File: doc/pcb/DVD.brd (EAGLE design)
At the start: 100 x 80 mm, 26 parts, among them IC1 7805, IC2 74HC14N

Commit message: PCB Board update
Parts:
- removed R10, R8, R9: (no value), resistor:0204/7
- added BNO055_1, SD_CARD: (no value), adafruit:1X06
- added BNO055_2: (no value), pinhead:1X04
- added NRF24L01: (no value), adafruit:2X04
- added POLULU_TB6612FNG: (no value), ic-package:DIL16
- JP10: value (none) -> STBY
- JP8: value (none) -> ENGINE2
- JP9: value (none) -> ENGINE1
- moved IC1 108.9 mm to (21.9, 81.3)
- moved JP7 91.4 mm to (30.0, 78.2)
- moved R3 91.1 mm to (30.1, 65.5), turned to 90 degrees
- moved JP5 82.3 mm to (26.3, 78.2)
- moved R7 82.2 mm to (33.9, 74.6), turned to 270 degrees
- moved JP9 79.6 mm to (43.7, 44.9)
- moved C1 79.4 mm to (15.4, 77.5)
- moved JP8 76.7 mm to (43.6, 41.9)
- moved JP3 73.5 mm to (1.60, 78.8)
- moved U$1 73.2 mm to (20.1, 56.8)
- moved R6 72.6 mm to (34.1, 65.6), turned to 90 degrees
- moved JP10 71.3 mm to (43.5, 47.5)
- moved IC2 68.7 mm to (40.3, 70.2), turned to 90 degrees
- moved JP6 66.3 mm to (28.4, 78.2)
- moved VS1838 63.4 mm to (43.8, 53.5), turned to 90 degrees
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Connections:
- removed net N$12: U$1.18/A4
- removed net N$13: U$1.19/A5
- removed net N$14: U$1.21/A7
- removed net N$15: U$1.22/A8
- removed net N$16: U$1.23/A9
- removed net N$23: U$1.14/A0
- removed net N$5: U$1.9
- removed net N$6: U$1.10
- removed net N$7: U$1.11
- removed net N$8: U$1.12
- new net CE: NRF24L01.3, U$1.8
- new net CSN_RADIO: NRF24L01.4, U$1.10
- new net CSN_SD: SD_CARD.1, U$1.9
- new net ENGINE1: JP9.1, POLULU_TB6612FNG.4, POLULU_TB6612FNG.5
- new net IN1: POLULU_TB6612FNG.12, POLULU_TB6612FNG.14, U$1.23/A9
- new net IN2: POLULU_TB6612FNG.11, POLULU_TB6612FNG.15, U$1.22/A8
- new net JP8: JP8.1, POLULU_TB6612FNG.3, POLULU_TB6612FNG.6
- new net MISO: NRF24L01.7, SD_CARD.4, U$1.12
- new net MOSI: NRF24L01.6, SD_CARD.3, U$1.11
- new net PWM: POLULU_TB6612FNG.10, POLULU_TB6612FNG.16, U$1.21/A7
- new net SCK: NRF24L01.5, SD_CARD.2, U$1.14/A0
- new net SCL: BNO055_1.5, U$1.19/A5
- new net SDA: BNO055_1.4, U$1.18/A4
- net +3V3: now also BNO055_1.1, NRF24L01.2, POLULU_TB6612FNG.2
- net +5V: now also SD_CARD.5
- net GND: now also BNO055_1.3, NRF24L01.1, POLULU_TB6612FNG.1, POLULU_TB6612FNG.8, POLULU_TB6612FNG.9, SD_CARD.6
- net N$4: now also JP10.1, POLULU_TB6612FNG.13; no longer U$1.8
- net V+: now also POLULU_TB6612FNG.7
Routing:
- net N$5: track 0.00 -> 170.0 mm

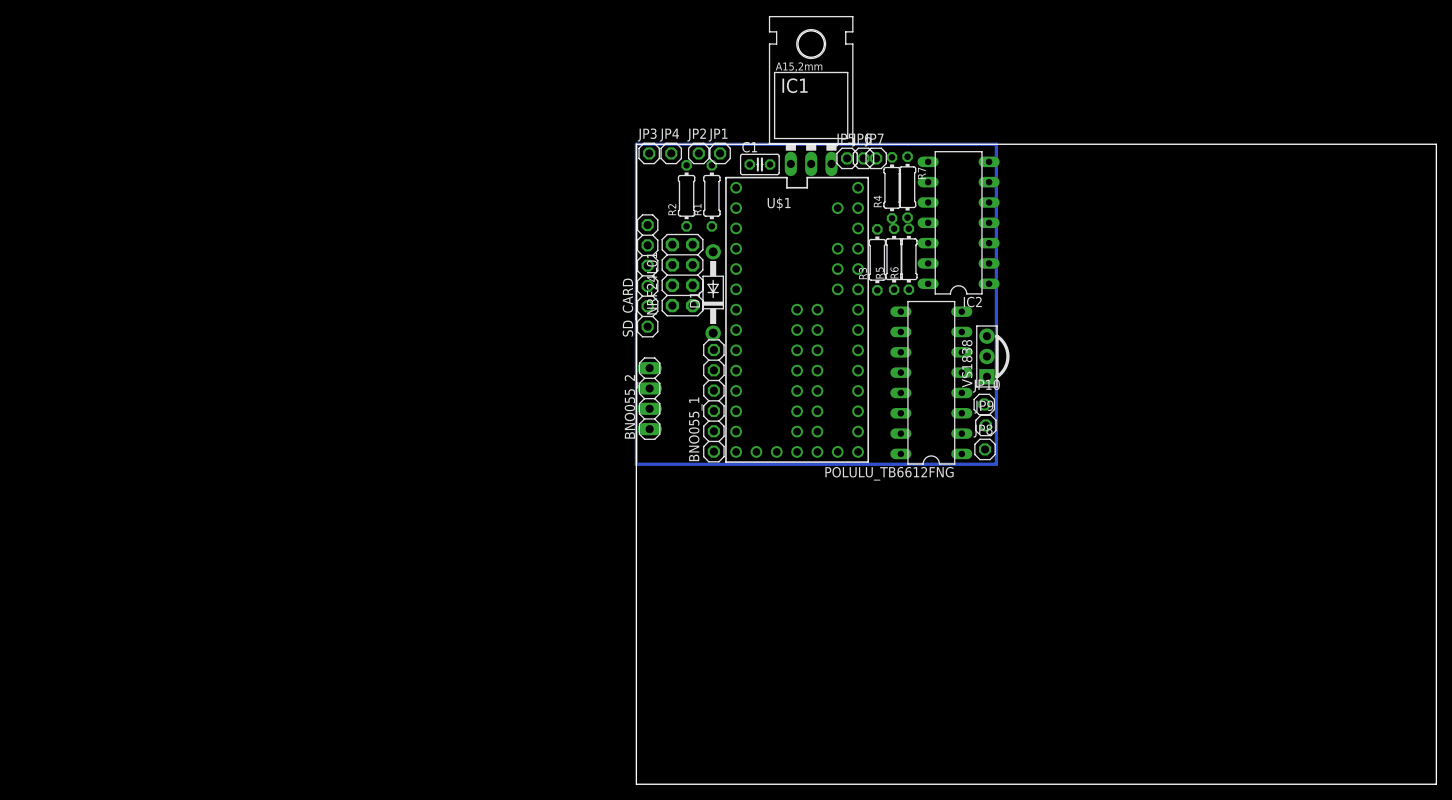
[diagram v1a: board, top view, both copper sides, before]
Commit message: Fixed Pololu/BNO055/Teensy footprint
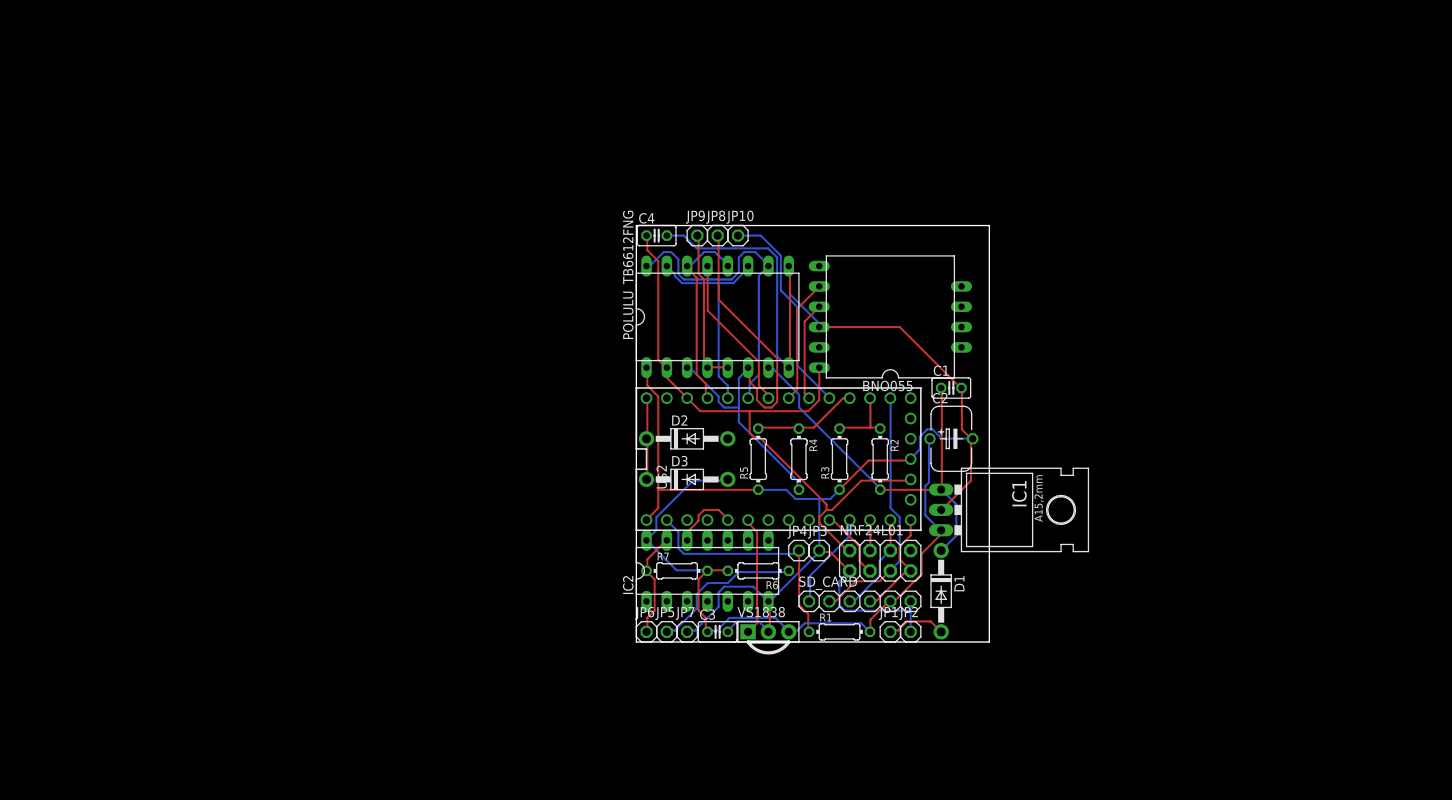
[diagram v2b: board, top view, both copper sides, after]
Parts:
- removed BNO055_1: (no value), adafruit:1X06
- removed BNO055_2: (no value), pinhead:1X04
- removed U$1: TEENSY_3.1_ALL_PINS_AND_PADS, Teensy_3_Series_Board_v1.0:TEENSY_3.1_ALLPINS
- added BNO055: (no value), ic-package_mod:DIL10-6-4
- added C2: 1000 uF, resistor:P128-50
- added C3: 100 nF, resistor:C025-025X050
- added C4: 100nF, resistor:C025-025X050
- added D2, D3: 1N4004, adafruit:DO41-10
- added U$2: TEENSY_3.1_BASIC, Teensy_3_Series_Board_v1.0:TEENSY_3.1_BASIC
- JP10: value STBY -> TEMP
- POLULU_TB6612FNG: value (none) -> DIL16W; device ic-package:DIL16 -> ic-package_mod:DIL16WIDE
- R2, R4: value 3K -> 3.3K
- moved JP2 65.4 mm to (34.3, 19.1)
- moved JP6 65.1 mm to (1.27, 19.1)
- moved JP7 63.7 mm to (6.35, 19.1)
- moved JP1 63.5 mm to (31.8, 19.1)
- moved JP5 63.3 mm to (3.81, 19.1)
- moved R1 56.8 mm to (25.4, 19.1), turned to 0 degrees
- moved R7 56.0 mm to (5.08, 26.7), turned to 0 degrees
- moved JP3 54.0 mm to (22.9, 29.2)
- moved IC2 53.7 mm to (8.89, 26.7), turned to 0 degrees
- moved JP4 52.1 mm to (20.3, 29.2)
- moved IC1 51.2 mm to (41.9, 34.3), turned to 270 degrees
- moved SD_CARD 48.6 mm to (27.9, 22.9), turned to 0 degrees
- moved D1 47.0 mm to (38.1, 24.1), turned to 270 degrees
- moved VS1838 43.9 mm to (16.5, 19.1), turned to 0 degrees
- moved NRF24L01 43.4 mm to (30.5, 27.9), turned to 0 degrees
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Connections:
- removed net AREF: U$1.AREF
- removed net N$24: U$1.17/A3
- removed net N$25: U$1.20/A6
- removed net N$29: R4.2
- removed net VCC: IC2.14
- removed net VUSB: U$1.VUSB
- new net JP0: JP10.1, U$2.17/A3
- new net N$5: D1.A, JP1.1
- new net STBY: POLULU_TB6612FNG.13, U$2.20/A6
- net +3V3: now also BNO055.1, C4.1, U$2.3.3V, U$2.3.3V1; no longer BNO055_1.1, U$1.3.3V, U$1.3.3V1, U$1.3.3V2
- net +5V: now also C2.+, C3.1, D3.A, IC2.14; no longer U$1.VIN
- net AGND: now also U$2.AGND; no longer U$1.AGND
- net CE: now also U$2.8; no longer U$1.8
- net CSN_RADIO: now also U$2.10; no longer U$1.10
- net CSN_SD: now also U$2.9; no longer U$1.9
- net D4_IR: now also U$2.4; no longer U$1.4
- net GND: now also BNO055.3, C2.-, C3.2, C4.2, U$2.GND, U$2.GND1; no longer BNO055_1.3, U$1.GND, U$1.GND1, U$1.GND2
- net IN1: now also U$2.23/A9; no longer U$1.23/A9
- net IN2: now also U$2.22/A8; no longer U$1.22/A8
- net JP8: now also R4.2
- net MISO: now also U$2.12; no longer U$1.12
- net MOSI: now also U$2.11; no longer U$1.11
- net N$1: now also D2.C, D3.C, U$2.VIN; no longer C1.1, D1.C, IC1.IN
- net N$10: now also U$2.15/A1; no longer U$1.15/A1
- net N$11: now also U$2.16/A2; no longer U$1.16/A2
- net N$18: now also U$2.0; no longer U$1.0
- net N$19: now also U$2.1; no longer U$1.1
- net N$20: now also U$2.2; no longer U$1.2
- net N$21: now also U$2.6; no longer U$1.6
- net N$22: now also U$2.7; no longer U$1.7
- net N$3: now also U$2.5; no longer U$1.5
- net N$4: now also D2.A; no longer JP10.1, POLULU_TB6612FNG.13
- net N$9: now also U$2.13; no longer U$1.13
- net PWM: now also U$2.21/A7; no longer U$1.21/A7
- net SCK: now also U$2.14/A0; no longer U$1.14/A0
- net SCL: now also BNO055.5, U$2.19/A5; no longer BNO055_1.5, U$1.19/A5
- net SDA: now also BNO055.4, U$2.18/A4; no longer BNO055_1.4, U$1.18/A4
- net SPEED_SENSOR: now also U$2.3; no longer U$1.3
- net V+: now also C1.1, D1.C, IC1.IN; no longer D1.A, JP1.1
- net VBAT: now also U$2.VBAT; no longer U$1.VBAT
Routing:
- net GND: track 0.00 -> 218.1 mm
- net N$5: track 170.0 -> 7.49 mm
- net +5V: track 0.00 -> 86.8 mm
- net +3V3: track 0.00 -> 80.6 mm
- net JP8: track 0.00 -> 59.5 mm
- net V+: track 0.00 -> 50.9 mm
- net PWM: track 0.00 -> 39.3 mm
- net SCK: track 0.00 -> 31.7 mm
- net N$18: track 0.00 -> 30.3 mm
- net IN2: track 0.00 -> 27.3 mm
- net JP0: track 0.00 -> 26.7 mm
- net IN1: track 0.00 -> 24.4 mm
- net ENGINE1: track 0.00 -> 19.8 mm
- net STBY: track 0.00 -> 19.8 mm
- net N$2: track 0.00 -> 19.5 mm
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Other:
- board size 100 x 80 mm -> 44.1 x 52.1 mm

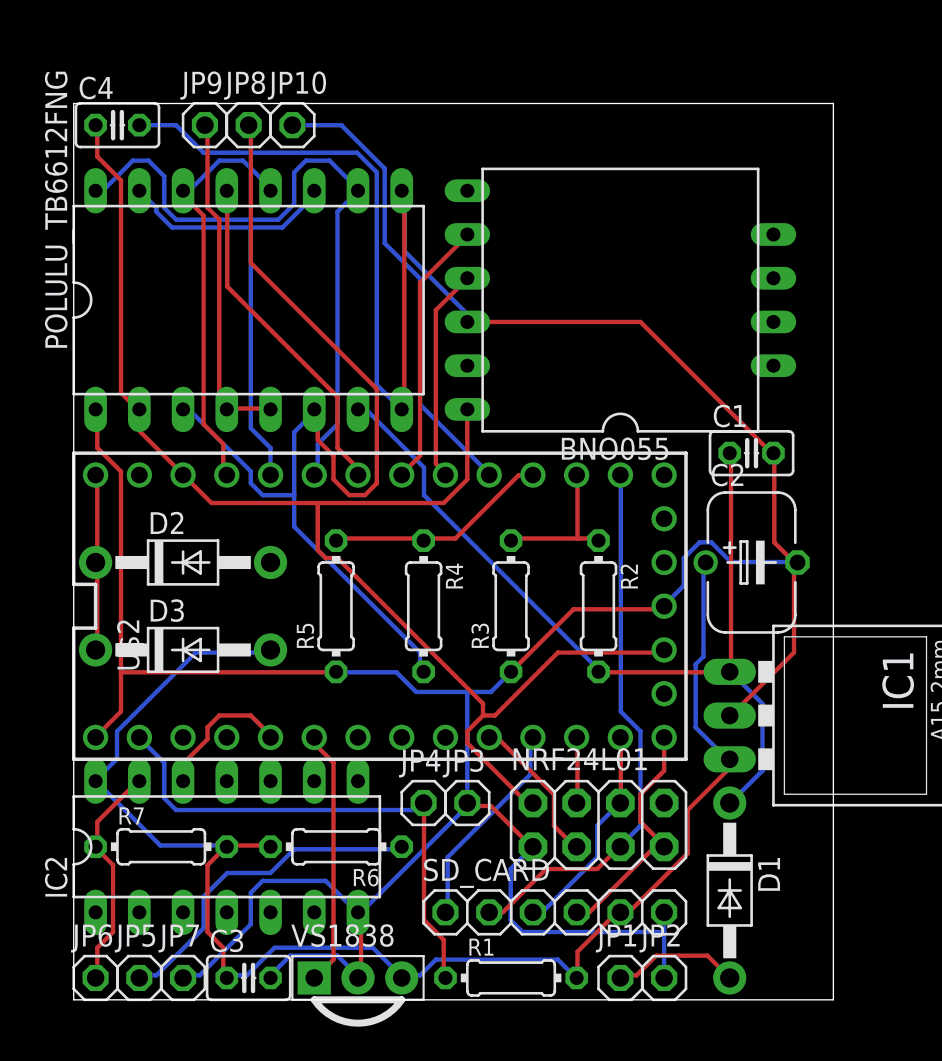
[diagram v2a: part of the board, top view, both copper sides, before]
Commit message: Fixed DR violations & added Copper Pour GND
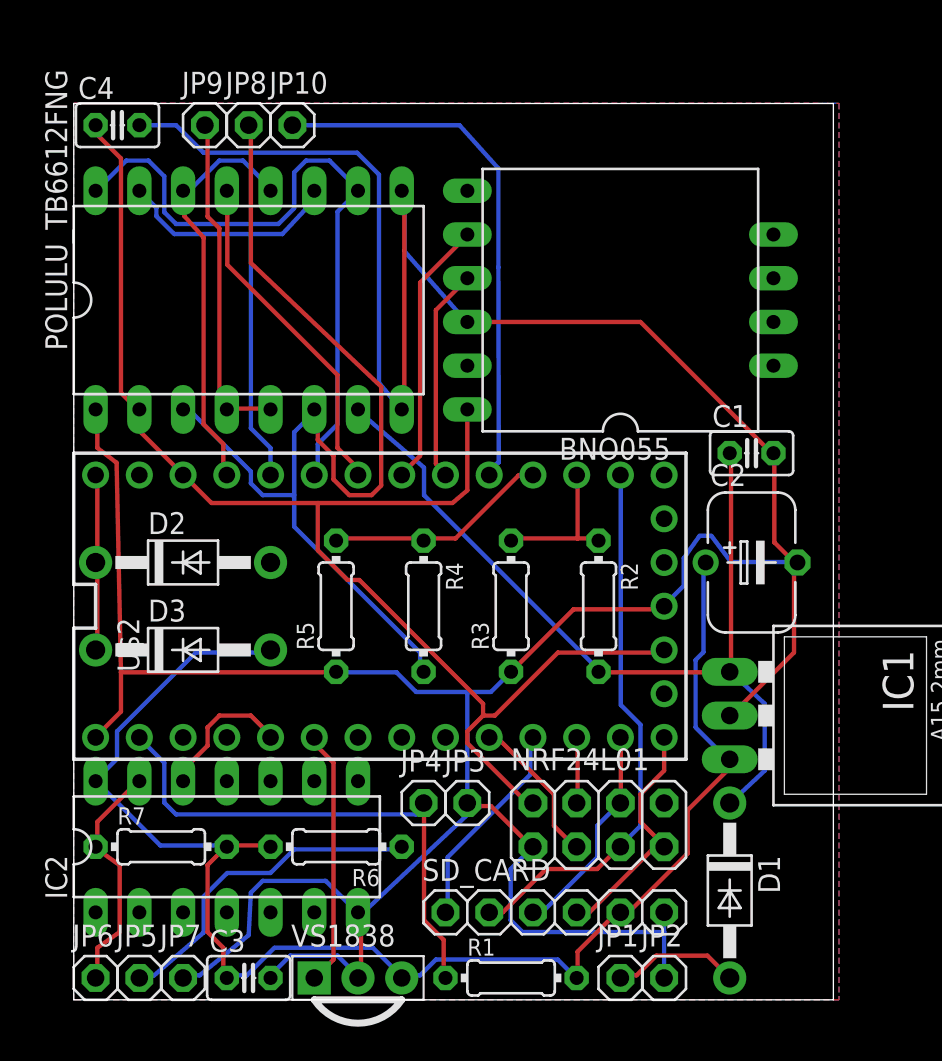
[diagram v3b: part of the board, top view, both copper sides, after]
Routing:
- net JP0: track 26.7 -> 31.3 mm
- net GND: track 218.1 -> 219.0 mm
- net N$26: track 13.3 -> 13.9 mm
- net JP8: track 59.5 -> 60.0 mm
- net PWM: track 39.3 -> 39.8 mm
- added copper zone on layer 1, net GND
- added copper zone on layer 16, net GND

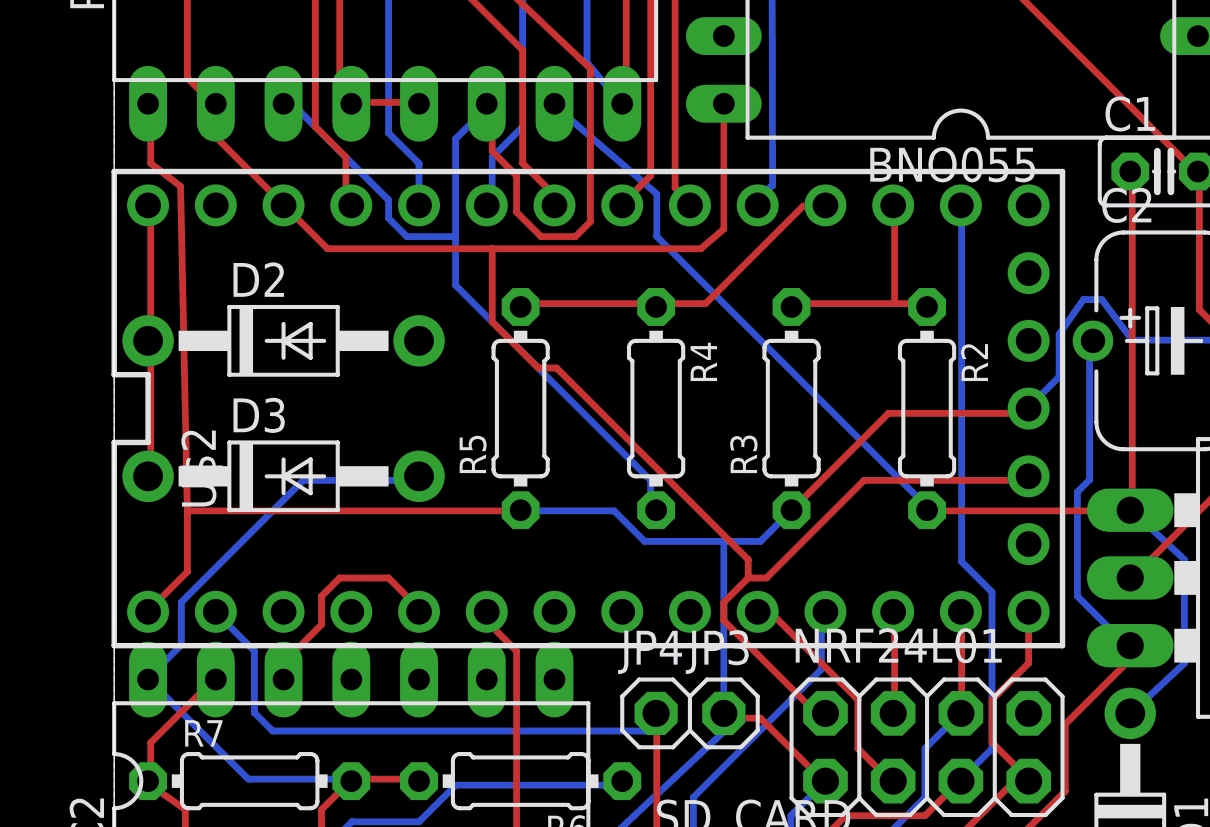
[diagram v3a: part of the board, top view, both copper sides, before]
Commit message: PCB removed not connected pins from Teensy
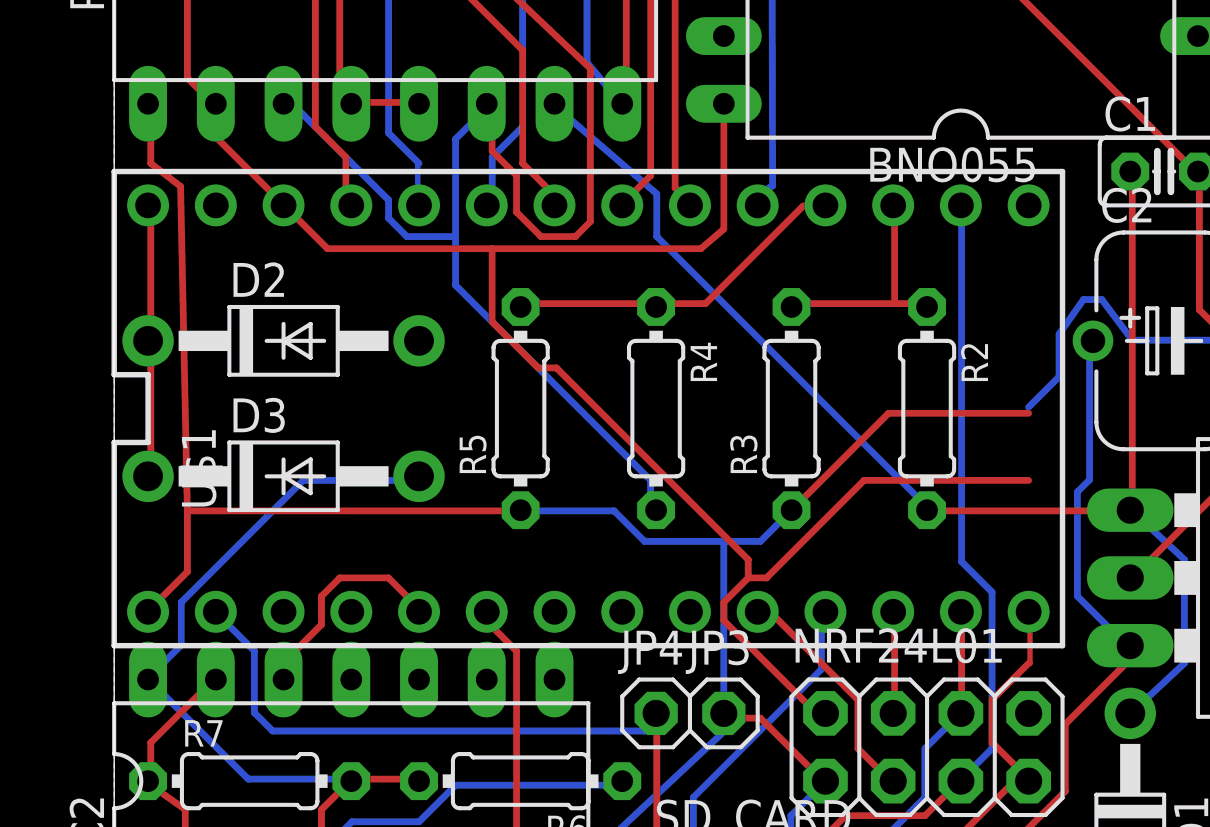
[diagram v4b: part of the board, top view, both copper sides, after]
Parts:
- removed U$2: TEENSY_3.1_BASIC, Teensy_3_Series_Board_v1.0:TEENSY_3.1_BASIC
- added U$1: TEENSY_3.1_BASIC_DVD, Teensy_3_Series_Board_v1.0:TEENSY_3.1_BASIC_DVD
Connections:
- removed net VBAT: U$2.VBAT
- net +3V3: now also U$1.3.3V; no longer U$2.3.3V, U$2.3.3V1
- net AGND: now also U$1.AGND; no longer U$2.AGND
- net CE: now also U$1.8; no longer U$2.8
- net CSN_RADIO: now also U$1.10; no longer U$2.10
- net CSN_SD: now also U$1.9; no longer U$2.9
- net D4_IR: now also U$1.4; no longer U$2.4
- net GND: now also U$1.GND; no longer U$2.GND, U$2.GND1
- net IN1: now also U$1.23/A9; no longer U$2.23/A9
- net IN2: now also U$1.22/A8; no longer U$2.22/A8
- net JP0: now also U$1.17/A3; no longer U$2.17/A3
- net MISO: now also U$1.12; no longer U$2.12
- net MOSI: now also U$1.11; no longer U$2.11
- net N$1: now also U$1.VIN; no longer U$2.VIN
- net N$10: now also U$1.15/A1; no longer U$2.15/A1
- net N$11: now also U$1.16/A2; no longer U$2.16/A2
- net N$18: now also U$1.0; no longer U$2.0
- net N$19: now also U$1.1; no longer U$2.1
- net N$20: now also U$1.2; no longer U$2.2
- net N$21: now also U$1.6; no longer U$2.6
- net N$22: now also U$1.7; no longer U$2.7
- net N$3: now also U$1.5; no longer U$2.5
- net N$9: now also U$1.13; no longer U$2.13
- net PWM: now also U$1.21/A7; no longer U$2.21/A7
- net SCK: now also U$1.14/A0; no longer U$2.14/A0
- net SCL: now also U$1.19/A5; no longer U$2.19/A5
- net SDA: now also U$1.18/A4; no longer U$2.18/A4
- net SPEED_SENSOR: now also U$1.3; no longer U$2.3
- net STBY: now also U$1.20/A6; no longer U$2.20/A6

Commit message: Created DVD.lbr for not existing parts and included them on PCB
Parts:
- removed BNO055: (no value), ic-package_mod:DIL10-6-4
- removed POLULU_TB6612FNG: DIL16W, ic-package_mod:DIL16WIDE
- added U$2: POLOLU_TB6612FNG, DVD:DIL16WIDE
- added U$4: BNO055, DVD:DIL10-6-4
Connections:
- new net 2/3V3OUT: U$4.2
- net +3V3: now also U$2.2, U$4.1; no longer BNO055.1, POLULU_TB6612FNG.2
- net ENGINE1: now also U$2.4, U$2.5; no longer POLULU_TB6612FNG.4, POLULU_TB6612FNG.5
- net GND: now also U$2.1, U$2.8, U$2.9, U$4.3; no longer BNO055.3, POLULU_TB6612FNG.1, POLULU_TB6612FNG.8, POLULU_TB6612FNG.9
- net IN1: now also U$2.12, U$2.14; no longer POLULU_TB6612FNG.12, POLULU_TB6612FNG.14
- net IN2: now also U$2.11, U$2.15; no longer POLULU_TB6612FNG.11, POLULU_TB6612FNG.15
- net JP8: now also U$2.3, U$2.6; no longer POLULU_TB6612FNG.3, POLULU_TB6612FNG.6
- net PWM: now also U$2.10, U$2.16; no longer POLULU_TB6612FNG.10, POLULU_TB6612FNG.16
- net SCL: now also U$4.5; no longer BNO055.5
- net SDA: now also U$4.4; no longer BNO055.4
- net STBY: now also U$2.13; no longer POLULU_TB6612FNG.13
- net V+: now also U$2.7; no longer POLULU_TB6612FNG.7
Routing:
- net GND: track 218.6 -> 186.2 mm
- net ENGINE1: track 19.8 -> 24.7 mm
- net JP8: track 60.0 -> 60.6 mm
- net PWM: track 39.9 -> 40.2 mm, vias 0 -> 1
